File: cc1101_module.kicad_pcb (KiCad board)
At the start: 4 copper layers, 30.7 x 33.1 mm, 34 parts, among them J1 SMA, Q1 BSS138, Q2 BSS138, Q3 BSS138, Q4 BSS138, U1 CC1101, U2 module_port_12pin, Y2 CX2016SA26000D0FLJG1

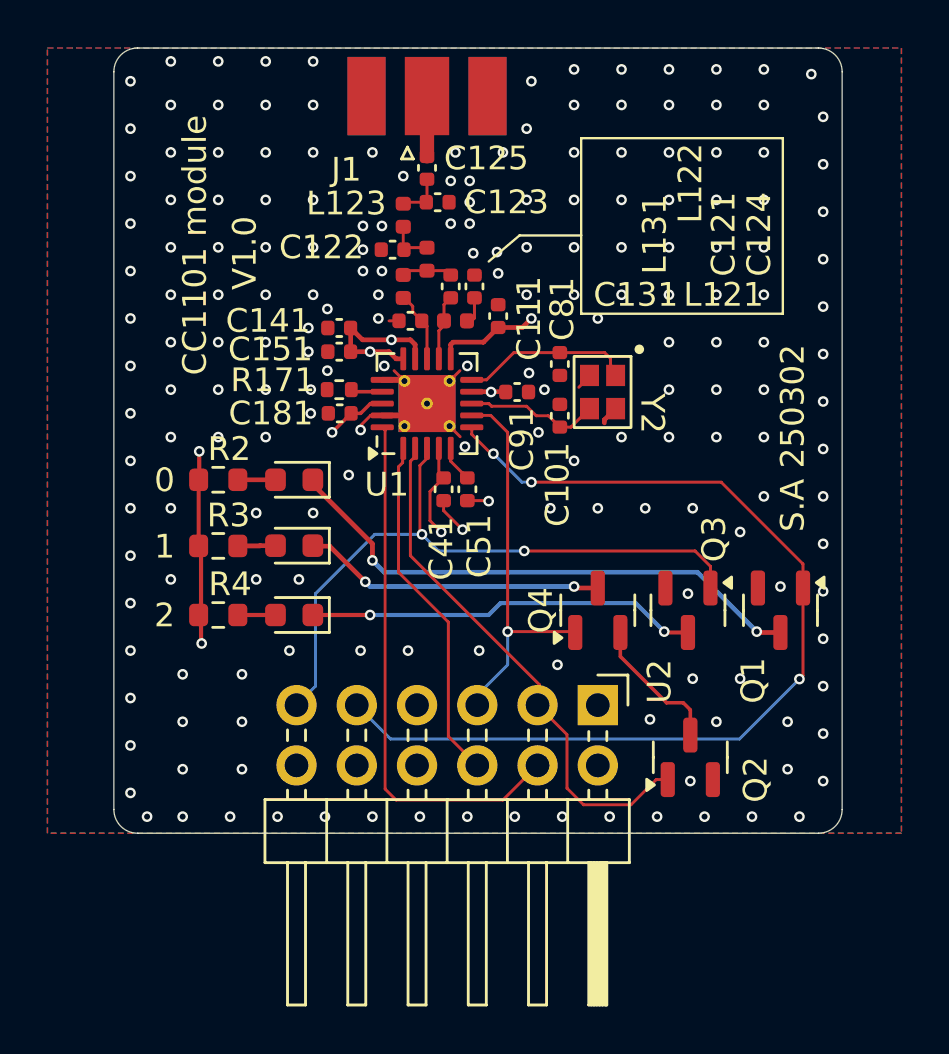
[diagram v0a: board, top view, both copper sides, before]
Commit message: Updated footprint for the oscillator
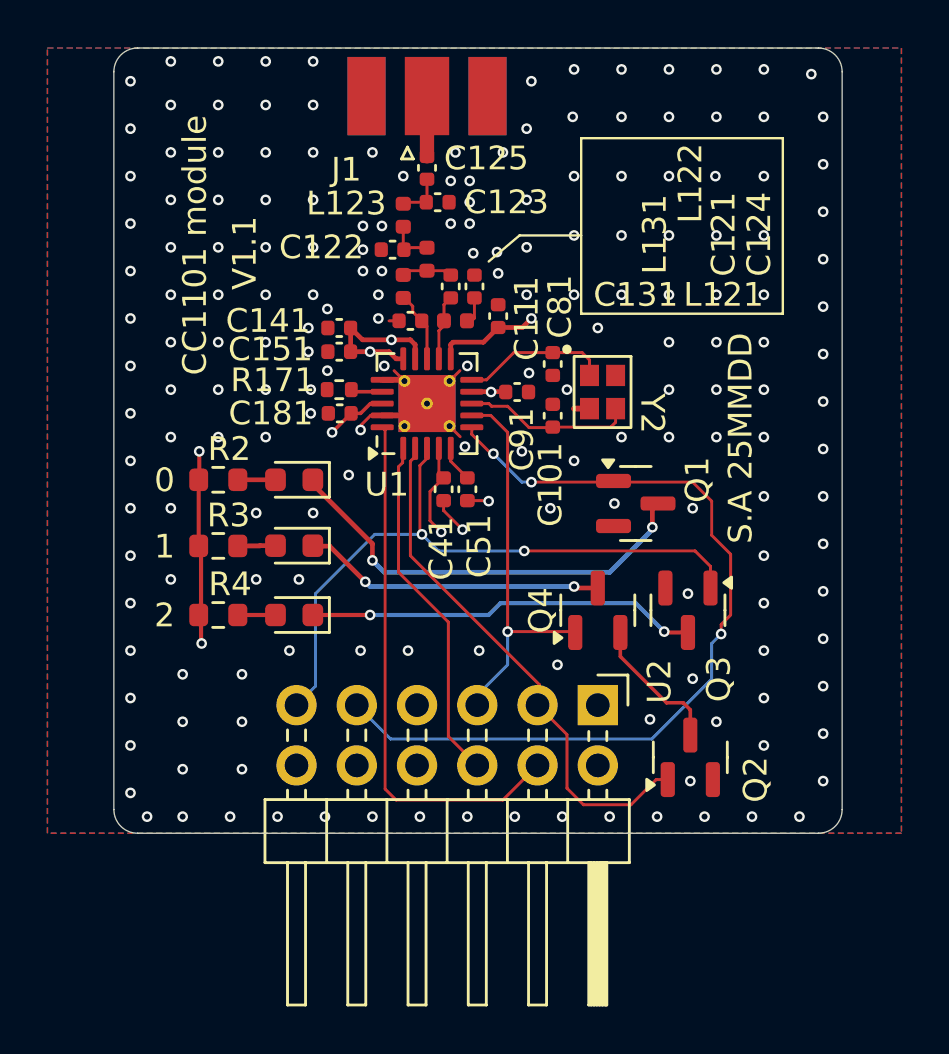
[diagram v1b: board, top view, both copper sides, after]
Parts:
- moved Q1 7.58 mm to (150.6, 88.8), turned to 0 degrees
- moved C101 0.30 mm to (147.1, 85.1)
- moved C81 0.30 mm to (147.1, 82.9)
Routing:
- net GDO_0: track 41.7 -> 36.3 mm
- net Net-(D3-K): track 22.9 -> 18.4 mm
- net Net-(U1-XOSC_Q1): track 5.68 -> 7.15 mm
- net Net-(U1-XOSC_Q2): track 7.23 -> 6.27 mm
- net GND: track 8.89 -> 8.05 mm, vias 193 -> 187
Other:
- board text added: "S.A 25MMDD"
- board text added: "V1.1"
- board text removed: "S.A 250302"
- board text removed: "V1.0"
